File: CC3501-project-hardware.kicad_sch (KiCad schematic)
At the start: 29 parts, among them J1 USB_C_Receptacle_USB2.0_16P, J3 Conn_01x03_Socket, Q1 AO3400A, U1 RP2040, U4 SY8089A1AAC

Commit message: Remove duplicated power flag.
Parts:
- renumbered J3 to J4
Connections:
- net +3.3V is gone; now on net +3V3: Q1.3 (D), R10.1
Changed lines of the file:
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@@
 	)
 	(symbol
-		(lib_id "power:+3.3V")
-		(at 54.61 149.86 0)
-		(unit 1)
-		(body_style 1)
-		(exclude_from_sim no)
-		(in_bom yes)
-		(on_board yes)
-		(in_pos_files yes)
-		(dnp no)
-		(fields_autoplaced yes)
-		(property "Reference" "#PWR015"
-			(at 54.61 153.67 0)
-			(hide yes)
-			(show_name no)
-			(do_not_autoplace no)
-			(effects
-				(font
-					(size 1.27 1.27)
-				)
-			)
-		)
-		(property "Value" "+3.3V"
-			(at 54.61 144.78 0)
-			(show_name no)
-			(do_not_autoplace no)
-			(effects
-				(font
-					(size 1.27 1.27)
-				)
-			)
-		)
-		(property "Footprint" ""
-			(at 54.61 149.86 0)
-			(hide yes)
-			(show_name no)
-			(do_not_autoplace no)
-			(effects
-				(font
-					(size 1.27 1.27)
-				)
-			)
-		)
-		(property "Datasheet" ""
-			(at 54.61 149.86 0)
-			(hide yes)
-			(show_name no)
-			(do_not_autoplace no)
-			(effects
-				(font
-					(size 1.27 1.27)
-				)
-			)
-		)
-		(property "Description" "Power symbol creates a global label with name \"+3.3V\""
-			(at 54.61 149.86 0)
-			(hide yes)
-			(show_name no)
-			(do_not_autoplace no)
-			(effects
-				(font
-					(size 1.27 1.27)
-				)
-			)
-		)
-		(pin "1"
-		)
-		(instances
-			(project "CC3501-project-hardware"
-				(path "/4a2d49bb-8ba4-4c60-a8f0-05b8d2544445"
-					(reference "#PWR015")
-					(unit 1)
-				)
-			)
-		)
-	)
-	(symbol
 		(lib_id "Device:C")
 		(at 236.22 154.94 0)
@@
 	)
 	(symbol
+		(lib_id "power:+3V3")
+		(at 40.64 165.1 0)
+		(unit 1)
+		(body_style 1)
+		(exclude_from_sim no)
+		(in_bom yes)
+		(on_board yes)
+		(in_pos_files yes)
+		(dnp no)
+		(fields_autoplaced yes)
+		(property "Reference" "#PWR016"
+			(at 40.64 168.91 0)
+			(hide yes)
+			(show_name no)
+			(do_not_autoplace no)
+			(effects
+				(font
+					(size 1.27 1.27)
+				)
+			)
+		)
+		(property "Value" "+3V3"
+			(at 40.64 160.02 0)
+			(show_name no)
+			(do_not_autoplace no)
+			(effects
+				(font
+					(size 1.27 1.27)
+				)
+			)
+		)
+		(property "Footprint" ""
+			(at 40.64 165.1 0)
+			(hide yes)
+			(show_name no)
+			(do_not_autoplace no)
+			(effects
+				(font
+					(size 1.27 1.27)
+				)
+			)
+		)
+		(property "Datasheet" ""
+			(at 40.64 165.1 0)
+			(hide yes)
+			(show_name no)
+			(do_not_autoplace no)
+			(effects
+				(font
+					(size 1.27 1.27)
+				)
+			)
+		)
+		(property "Description" "Power symbol creates a global label with name \"+3V3\""
+			(at 40.64 165.1 0)
+			(hide yes)
+			(show_name no)
+			(do_not_autoplace no)
+			(effects
+				(font
+					(size 1.27 1.27)
+				)
+			)
+		)
+		(pin "1"
+		)
+		(instances
+			(project "CC3501-project-hardware"
+				(path "/4a2d49bb-8ba4-4c60-a8f0-05b8d2544445"
+					(reference "#PWR016")
+					(unit 1)
+				)
+			)
+		)
+	)
+	(symbol
 		(lib_id "Device:C")
 		(at 266.7 154.94 0)
@@
 	)
 	(symbol
-		(lib_id "power:+3.3V")
-		(at 40.64 165.1 0)
-		(unit 1)
-		(body_style 1)
-		(exclude_from_sim no)
-		(in_bom yes)
-		(on_board yes)
-		(in_pos_files yes)
-		(dnp no)
-		(property "Reference" "#PWR016"
-			(at 40.64 168.91 0)
-			(hide yes)
-			(show_name no)
-			(do_not_autoplace no)
-			(effects
-				(font
-					(size 1.27 1.27)
-				)
-			)
-		)
-		(property "Value" "+3.3V"
-			(at 40.64 161.29 0)
-			(show_name no)
-			(do_not_autoplace no)
-			(effects
-				(font
-					(size 1.27 1.27)
-				)
-			)
-		)
-		(property "Footprint" ""
-			(at 40.64 165.1 0)
-			(hide yes)
-			(show_name no)
-			(do_not_autoplace no)
-			(effects
-				(font
-					(size 1.27 1.27)
-				)
-			)
-		)
-		(property "Datasheet" ""
-			(at 40.64 165.1 0)
-			(hide yes)
-			(show_name no)
-			(do_not_autoplace no)
-			(effects
-				(font
-					(size 1.27 1.27)
-				)
-			)
-		)
-		(property "Description" "Power symbol creates a global label with name \"+3.3V\""
-			(at 40.64 165.1 0)
-			(hide yes)
-			(show_name no)
-			(do_not_autoplace no)
-			(effects
-				(font
-					(size 1.27 1.27)
-				)
-			)
-		)
-		(pin "1"
-		)
-		(instances
-			(project "CC3501-project-hardware"
-				(path "/4a2d49bb-8ba4-4c60-a8f0-05b8d2544445"
-					(reference "#PWR016")
-					(unit 1)
-				)
-			)
-		)
-	)
-	(symbol
 		(lib_id "power:GND")
 		(at 215.9 158.75 0)
@@
 	)
 	(symbol
+		(lib_id "power:+3V3")
+		(at 54.61 149.86 0)
+		(unit 1)
+		(body_style 1)
+		(exclude_from_sim no)
+		(in_bom yes)
+		(on_board yes)
+		(in_pos_files yes)
+		(dnp no)
+		(fields_autoplaced yes)
+		(property "Reference" "#PWR015"
+			(at 54.61 153.67 0)
+			(hide yes)
+			(show_name no)
+			(do_not_autoplace no)
+			(effects
+				(font
+					(size 1.27 1.27)
+				)
+			)
+		)
+		(property "Value" "+3V3"
+			(at 54.61 144.78 0)
+			(show_name no)
+			(do_not_autoplace no)
+			(effects
+				(font
+					(size 1.27 1.27)
+				)
+			)
+		)
+		(property "Footprint" ""
+			(at 54.61 149.86 0)
+			(hide yes)
+			(show_name no)
+			(do_not_autoplace no)
+			(effects
+				(font
+					(size 1.27 1.27)
+				)
+			)
+		)
+		(property "Datasheet" ""
+			(at 54.61 149.86 0)
+			(hide yes)
+			(show_name no)
+			(do_not_autoplace no)
+			(effects
+				(font
+					(size 1.27 1.27)
+				)
+			)
+		)
+		(property "Description" "Power symbol creates a global label with name \"+3V3\""
+			(at 54.61 149.86 0)
+			(hide yes)
+			(show_name no)
+			(do_not_autoplace no)
+			(effects
+				(font
+					(size 1.27 1.27)
+				)
+			)
+		)
+		(pin "1"
+		)
+		(instances
+			(project "CC3501-project-hardware"
+				(path "/4a2d49bb-8ba4-4c60-a8f0-05b8d2544445"
+					(reference "#PWR015")
+					(unit 1)
+				)
+			)
+		)
+	)
+	(symbol
 		(lib_id "power:+1V1")
 		(at 193.04 151.13 0)
@@
 		(dnp no)
 		(fields_autoplaced yes)
-		(property "Reference" "J3"
+		(property "Reference" "J4"
 			(at 72.39 143.51 90)
 			(show_name no)
@@
 			(project "CC3501-project-hardware"
 				(path "/4a2d49bb-8ba4-4c60-a8f0-05b8d2544445"
-					(reference "J3")
+					(reference "J4")
 					(unit 1)
 				)

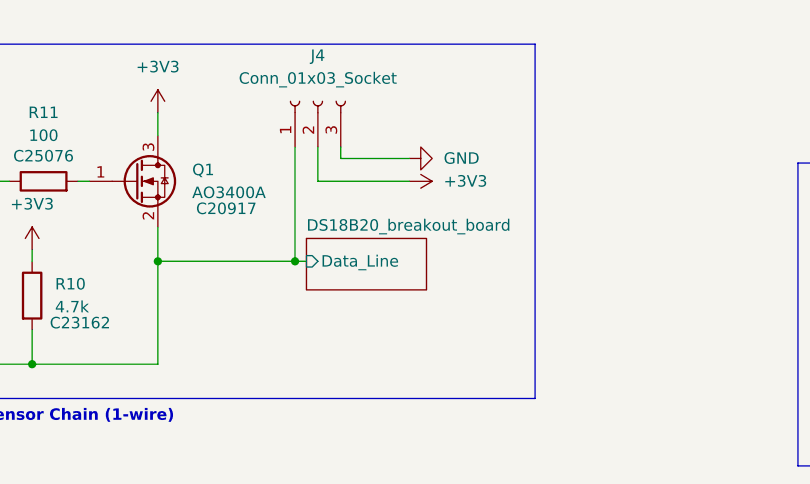
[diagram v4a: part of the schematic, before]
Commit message: Change wiring on temp sensor.
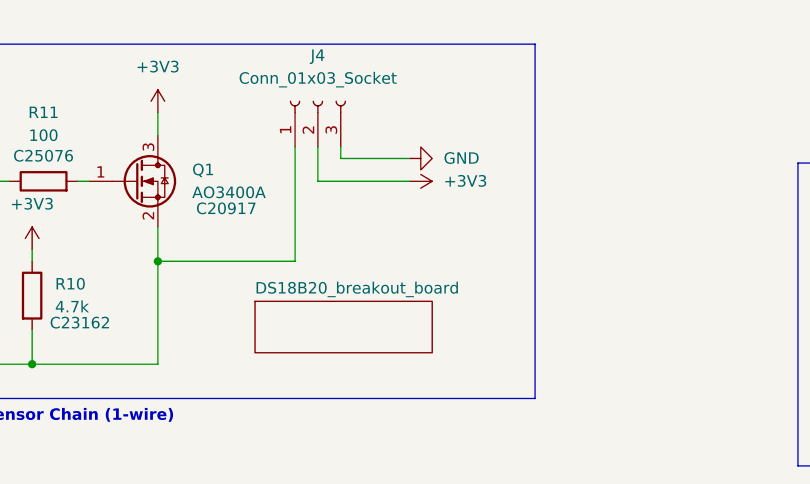
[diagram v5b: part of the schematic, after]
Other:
- sheet DS18B20_breakout_board ports: added none; removed Data_Line
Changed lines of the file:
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@@
 	)
 	(junction
-		(at 69.85 166.37)
-		(diameter 0)
-		(color 0 0 0 0)
-	)
-	(junction
 		(at 215.9 35.56)
 		(diameter 0)
@@
 	(wire
 		(pts
-			(xy 69.85 166.37) (xy 71.12 166.37)
-		)
-		(stroke
-			(width 0)
-			(type default)
-		)
-	)
-	(wire
-		(pts
 			(xy 166.37 106.68) (xy 168.91 106.68)
 		)
@@
 	)
 	(sheet
-		(at 71.12 163.83)
-		(size 13.335 5.715)
+		(at 65.405 170.815)
+		(size 19.685 5.715)
 		(exclude_from_sim no)
 		(in_bom yes)
@@
 		)
 		(property "Sheetname" "DS18B20_breakout_board"
-			(at 71.12 163.1184 0)
+			(at 65.405 170.1034 0)
 			(show_name no)
 			(do_not_autoplace no)
@@
 		)
 		(property "Sheetfile" "DS18B20_Breakout_Board.kicad_sch"
-			(at 71.12 170.1296 0)
+			(at 65.405 177.1146 0)
 			(hide yes)
 			(show_name no)
@@
 			)
 		)
-		(pin "Data_Line" input
-			(at 71.12 166.37 180)
-			(effects
-				(font
-					(size 1.27 1.27)
-				)
-				(justify left)
-			)
-		)

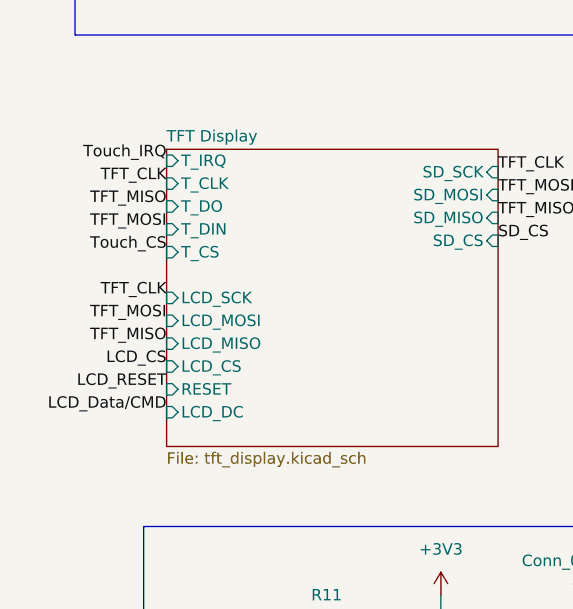
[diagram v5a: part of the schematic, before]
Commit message: Rewire TFT display to power with 5V and allowing backlight switching via FET.
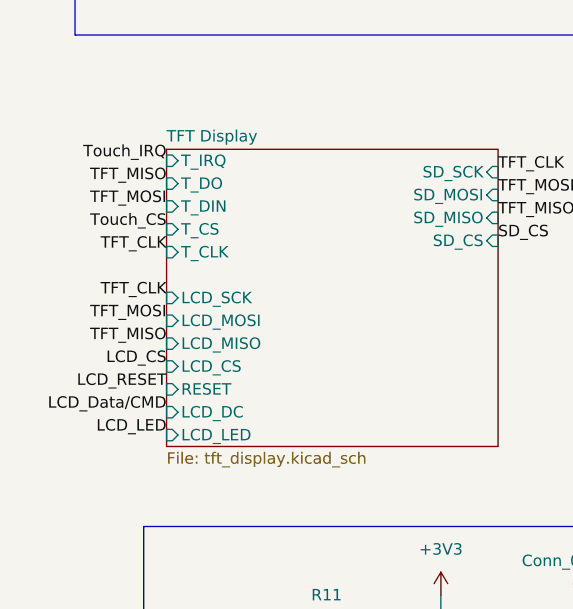
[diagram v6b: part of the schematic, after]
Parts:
- J1: footprint Connector_PinSocket_2.54mm:PinSocket_1x03_P2.54mm_Vertical -> Connector_USB:USB_C_Receptacle_G-Switch_GT-USB-7010ASV
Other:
- sheet TFT Display ports: added LCD_LED; removed none
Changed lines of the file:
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@@
 	)
 	(label "TFT_CLK"
-		(at 24.13 104.14 180)
+		(at 24.13 111.76 180)
 		(effects
 			(font
@@
 	)
 	(label "TFT_MOSI"
-		(at 24.13 109.22 180)
+		(at 24.13 106.68 180)
 		(effects
 			(font
@@
 		)
 	)
+	(label "LCD_LED"
+		(at 24.13 132.08 180)
+		(effects
+			(font
+				(size 1.27 1.27)
+			)
+			(justify right bottom)
+		)
+	)
 	(label "TFT_CLK"
 		(at 60.96 102.87 0)
@@
 	)
 	(label "Touch_CS"
-		(at 24.13 111.76 180)
+		(at 24.13 109.22 180)
 		(effects
 			(font
@@
 	)
 	(label "TFT_MISO"
-		(at 24.13 106.68 180)
+		(at 24.13 104.14 180)
 		(effects
 			(font
@@
 			)
 		)
-		(property "Footprint" "Connector_PinSocket_2.54mm:PinSocket_1x03_P2.54mm_Vertical"
+		(property "Footprint" "Connector_USB:USB_C_Receptacle_G-Switch_GT-USB-7010ASV"
 			(at 34.29 46.99 0)
 			(hide yes)
@@
 		)
 		(pin "T_CLK" input
-			(at 24.13 104.14 180)
+			(at 24.13 111.76 180)
 			(effects
 				(font
@@
 		)
 		(pin "T_DO" input
-			(at 24.13 106.68 180)
+			(at 24.13 104.14 180)
 			(effects
 				(font
@@
 		)
 		(pin "T_CS" input
-			(at 24.13 111.76 180)
+			(at 24.13 109.22 180)
 			(effects
 				(font
@@
 		)
 		(pin "T_DIN" input
-			(at 24.13 109.22 180)
+			(at 24.13 106.68 180)
 			(effects
 				(font
@@
 			)
 		)
+		(pin "LCD_LED" input
+			(at 24.13 132.08 180)
+			(effects
+				(font
+					(size 1.27 1.27)
+				)
+				(justify left)
+			)
+		)

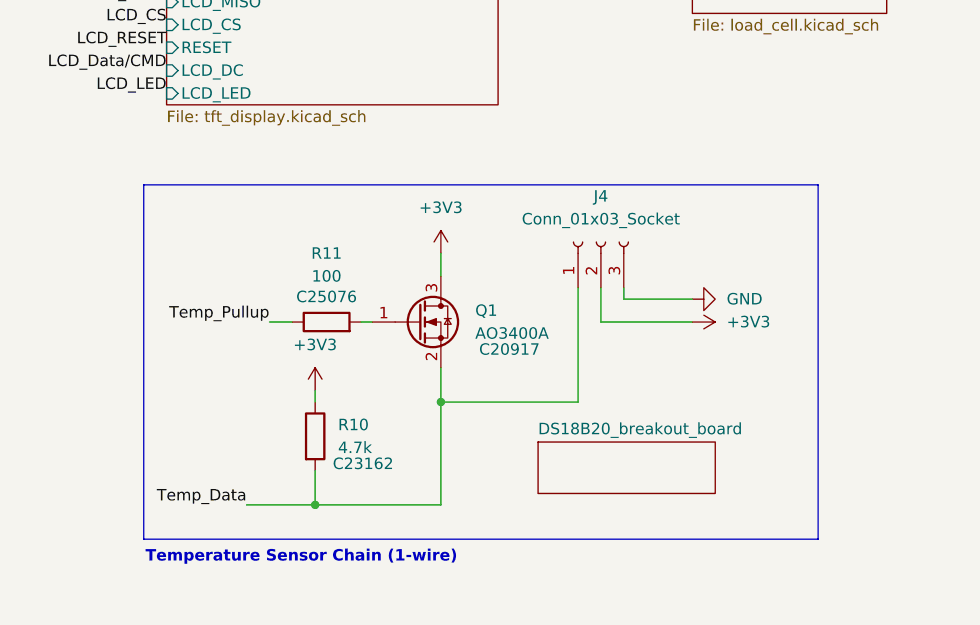
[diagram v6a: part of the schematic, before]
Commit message: update passive power FET from N-CH to P-CH as recommended from peer review.
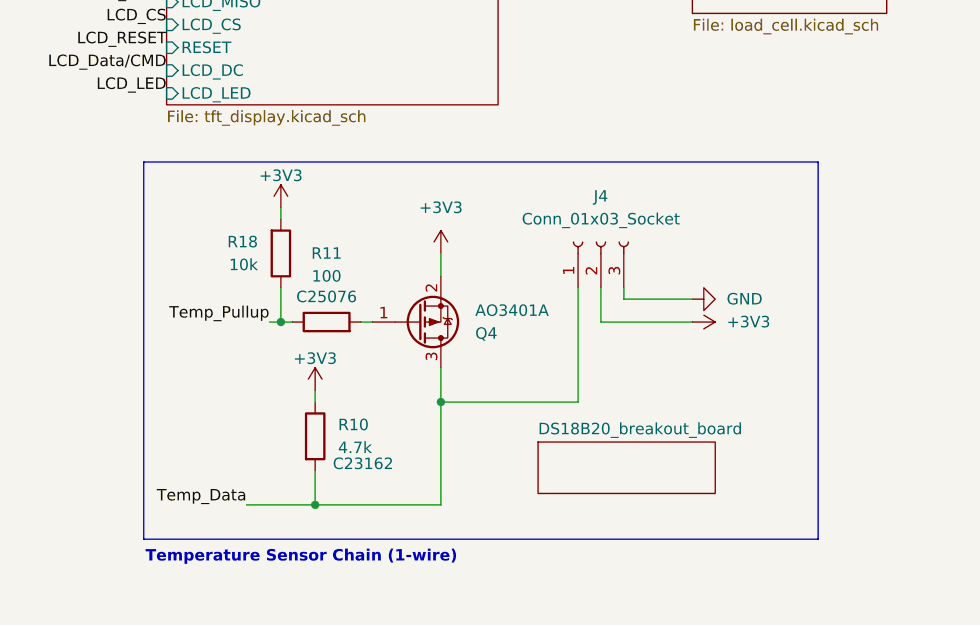
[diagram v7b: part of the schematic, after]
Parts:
- removed Q1: AO3400A, Package_TO_SOT_SMD:SOT-23, symbol Transistor_FET:AO3400A
- added Q4: AO3401A, Package_TO_SOT_SMD:SOT-23, symbol Transistor_FET:AO3401A
- added R18: 10k, Resistor_SMD:R_0805_2012Metric, symbol Device:R
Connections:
- net +3V3: now also Q4.2 (S), R18.2
- net Temp_Data: now also Q4.3 (D)
- net Temp_Pullup: now also R18.1
- net at R11.2: now also Q4.1 (G)
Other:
- sheet RFID: file RFID\CE-PiicoDev-RFID-Reader-Writer.kicad_sch -> RFID/CE-PiicoDev-RFID-Reader-Writer.kicad_sch

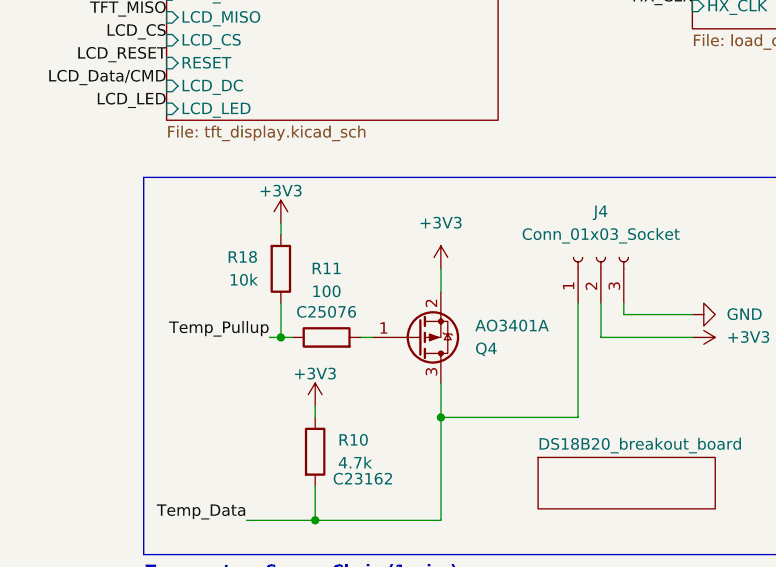
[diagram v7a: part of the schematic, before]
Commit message: edit HX711 configuration to match datasheet and sparkfun example as well as add JLC part numbers and display them on schematic
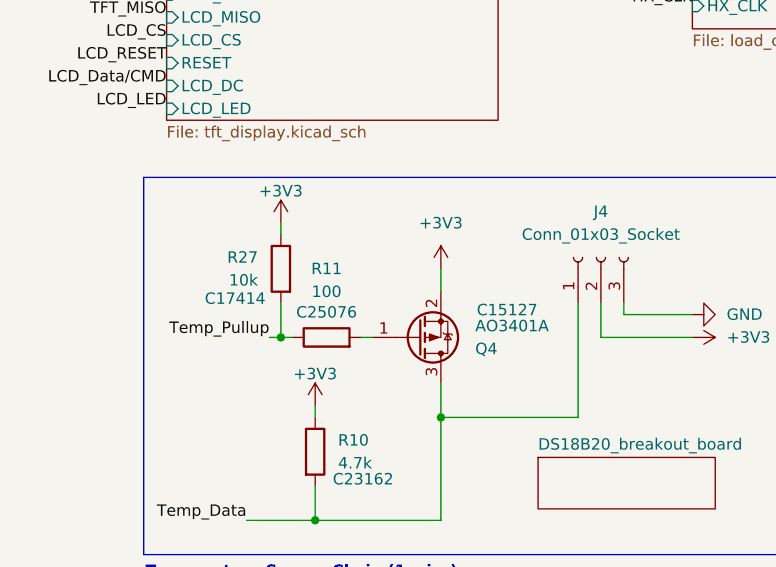
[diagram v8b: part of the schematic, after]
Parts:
- removed R18: 10k, Resistor_SMD:R_0805_2012Metric, symbol Device:R
- added R27: 10k, Resistor_SMD:R_0805_2012Metric, symbol Device:R
- Q4: LCSC PN (none) -> C15127
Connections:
- net +3V3: now also R27.1
- net Temp_Pullup: now also R27.2
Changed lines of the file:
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@@
 	)
 	(symbol
-		(lib_id "Device:R")
-		(at 36.83 149.86 0)
-		(mirror x)
-		(unit 1)
-		(body_style 1)
-		(exclude_from_sim no)
-		(in_bom yes)
-		(on_board yes)
-		(in_pos_files yes)
-		(dnp no)
-		(fields_autoplaced yes)
-		(property "Reference" "R18"
-			(at 34.29 148.5899 0)
-			(show_name no)
-			(do_not_autoplace no)
-			(effects
-				(font
-					(size 1.27 1.27)
-				)
-				(justify right)
-			)
-		)
-		(property "Value" "10k"
-			(at 34.29 151.1299 0)
-			(show_name no)
-			(do_not_autoplace no)
-			(effects
-				(font
-					(size 1.27 1.27)
-				)
-				(justify right)
-			)
-		)
-		(property "Footprint" "Resistor_SMD:R_0805_2012Metric"
-			(at 35.052 149.86 90)
-			(hide yes)
-			(show_name no)
-			(do_not_autoplace no)
-			(effects
-				(font
-					(size 1.27 1.27)
-				)
-			)
-		)
-		(property "Datasheet" ""
-			(at 36.83 149.86 0)
-			(hide yes)
-			(show_name no)
-			(do_not_autoplace no)
-			(effects
-				(font
-					(size 1.27 1.27)
-				)
-			)
-		)
-		(property "Description" "Resistor"
-			(at 36.83 149.86 0)
-			(hide yes)
-			(show_name no)
-			(do_not_autoplace no)
-			(effects
-				(font
-					(size 1.27 1.27)
-				)
-			)
-		)
-		(property "LCSC PN" "C17414"
-			(at 36.83 149.86 0)
-			(hide yes)
-			(show_name no)
-			(do_not_autoplace no)
-			(effects
-				(font
-					(size 1.27 1.27)
-				)
-			)
-		)
-		(pin "1"
-		)
-		(pin "2"
-		)
-		(instances
-			(project "CC3501-project-hardware"
-				(path "/4a2d49bb-8ba4-4c60-a8f0-05b8d2544445"
-					(reference "R18")
-					(unit 1)
-				)
-			)
-		)
-	)
-	(symbol
 		(lib_id "Device:C")
 		(at 266.7 154.94 0)
@@
 	)
 	(symbol
+		(lib_id "Device:R")
+		(at 36.83 149.86 0)
+		(mirror y)
+		(unit 1)
+		(body_style 1)
+		(exclude_from_sim no)
+		(in_bom yes)
+		(on_board yes)
+		(in_pos_files yes)
+		(dnp no)
+		(property "Reference" "R27"
+			(at 34.29 148.5899 0)
+			(show_name no)
+			(do_not_autoplace no)
+			(effects
+				(font
+					(size 1.27 1.27)
+				)
+				(justify left)
+			)
+		)
+		(property "Value" "10k"
+			(at 34.29 151.1299 0)
+			(show_name no)
+			(do_not_autoplace no)
+			(effects
+				(font
+					(size 1.27 1.27)
+				)
+				(justify left)
+			)
+		)
+		(property "Footprint" "Resistor_SMD:R_0805_2012Metric"
+			(at 38.608 149.86 90)
+			(hide yes)
+			(show_name no)
+			(do_not_autoplace no)
+			(effects
+				(font
+					(size 1.27 1.27)
+				)
+			)
+		)
+		(property "Datasheet" ""
+			(at 36.83 149.86 0)
+			(hide yes)
+			(show_name no)
+			(do_not_autoplace no)
+			(effects
+				(font
+					(size 1.27 1.27)
+				)
+			)
+		)
+		(property "Description" "Resistor"
+			(at 36.83 149.86 0)
+			(hide yes)
+			(show_name no)
+			(do_not_autoplace no)
+			(effects
+				(font
+					(size 1.27 1.27)
+				)
+			)
+		)
+		(property "LCSC PN" "C17414"
+			(at 31.75 153.162 0)
+			(show_name no)
+			(do_not_autoplace no)
+			(effects
+				(font
+					(size 1.27 1.27)
+				)
+			)
+		)
+		(property "CAPACITANCE" ""
+			(at 36.83 149.86 0)
+			(hide yes)
+			(show_name no)
+			(do_not_autoplace no)
+			(effects
+				(font
+					(size 1.27 1.27)
+				)
+			)
+		)
+		(property "CASE SIZE/DIMENSION" ""
+			(at 36.83 149.86 0)
+			(hide yes)
+			(show_name no)
+			(do_not_autoplace no)
+			(effects
+				(font
+					(size 1.27 1.27)
+				)
+			)
+		)
+		(property "DATASHEET URL" ""
+			(at 36.83 149.86 0)
+			(hide yes)
+			(show_name no)
+			(do_not_autoplace no)
+			(effects
+				(font
+					(size 1.27 1.27)
+				)
+			)
+		)
+		(property "DATASHEET VERSION" ""
+			(at 36.83 149.86 0)
+			(hide yes)
+			(show_name no)
+			(do_not_autoplace no)
+			(effects
+				(font
+					(size 1.27 1.27)
+				)
+			)
+		)
+		(property "DIELECTRIC" ""
+			(at 36.83 149.86 0)
+			(hide yes)
+			(show_name no)
+			(do_not_autoplace no)
+			(effects
+				(font
+					(size 1.27 1.27)
+				)
+			)
+		)
+		(property "MANUFACTURER URL" ""
+			(at 36.83 149.86 0)
+			(hide yes)
+			(show_name no)
+			(do_not_autoplace no)
+			(effects
+				(font
+					(size 1.27 1.27)
+				)
+			)
+		)
+		(property "RATED VOLTAGE" ""
+			(at 36.83 149.86 0)
+			(hide yes)
+			(show_name no)
+			(do_not_autoplace no)
+			(effects
+				(font
+					(size 1.27 1.27)
+				)
+			)
+		)
+		(property "TOLERANCE (%)" ""
+			(at 36.83 149.86 0)
+			(hide yes)
+			(show_name no)
+			(do_not_autoplace no)
+			(effects
+				(font
+					(size 1.27 1.27)
+				)
+			)
+		)
+		(property "KLC_S3.3" ""
+			(at 36.83 149.86 0)
+			(hide yes)
+			(show_name no)
+			(do_not_autoplace no)
+			(effects
+				(font
+					(size 1.27 1.27)
+				)
+			)
+		)
+		(property "KLC_S4.1" ""
+			(at 36.83 149.86 0)
+			(hide yes)
+			(show_name no)
+			(do_not_autoplace no)
+			(effects
+				(font
+					(size 1.27 1.27)
+				)
+			)
+		)
+		(pin "2"
+		)
+		(pin "1"
+		)
+		(instances
+			(project "CC3501-project-hardware"
+				(path "/4a2d49bb-8ba4-4c60-a8f0-05b8d2544445"
+					(reference "R27")
+					(unit 1)
+				)
+			)
+		)
+	)
+	(symbol
 		(lib_id "power:GND")
 		(at 200.66 54.61 0)
@@
 			)
 		)
-		(property "LCSC PN" ""
-			(at 52.07 157.48 0)
-			(hide yes)
+		(property "LCSC PN" "C15127"
+			(at 61.976 154.432 0)
 			(show_name no)
 			(do_not_autoplace no)
